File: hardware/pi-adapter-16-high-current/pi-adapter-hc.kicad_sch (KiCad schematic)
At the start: 33 parts, among them J1 Conn_02x02_Odd_Even, P1 CONN_01X04, P10 CONN_01X04, P11 CONN_01X04, P12 CONN_01X04, P13 CONN_01X04, P14 CONN_01X04, P15 CONN_01X04, P16 CONN_01X04, P17 5V, P2 CONN_01X04, P20 CONN_02X20, P21 I2C, P22 System SPI, P23 UART, P3 CONN_01X04, P30 +5V, P31 GND, P4 CONN_01X04, P5 CONN_01X04, P6 CONN_01X04, P7 CONN_01X04, P8 CONN_01X04, P9 CONN_01X04, U1 74AHCT245, U2 74AHCT245, U3 74AHCT245, U4 74AHCT245

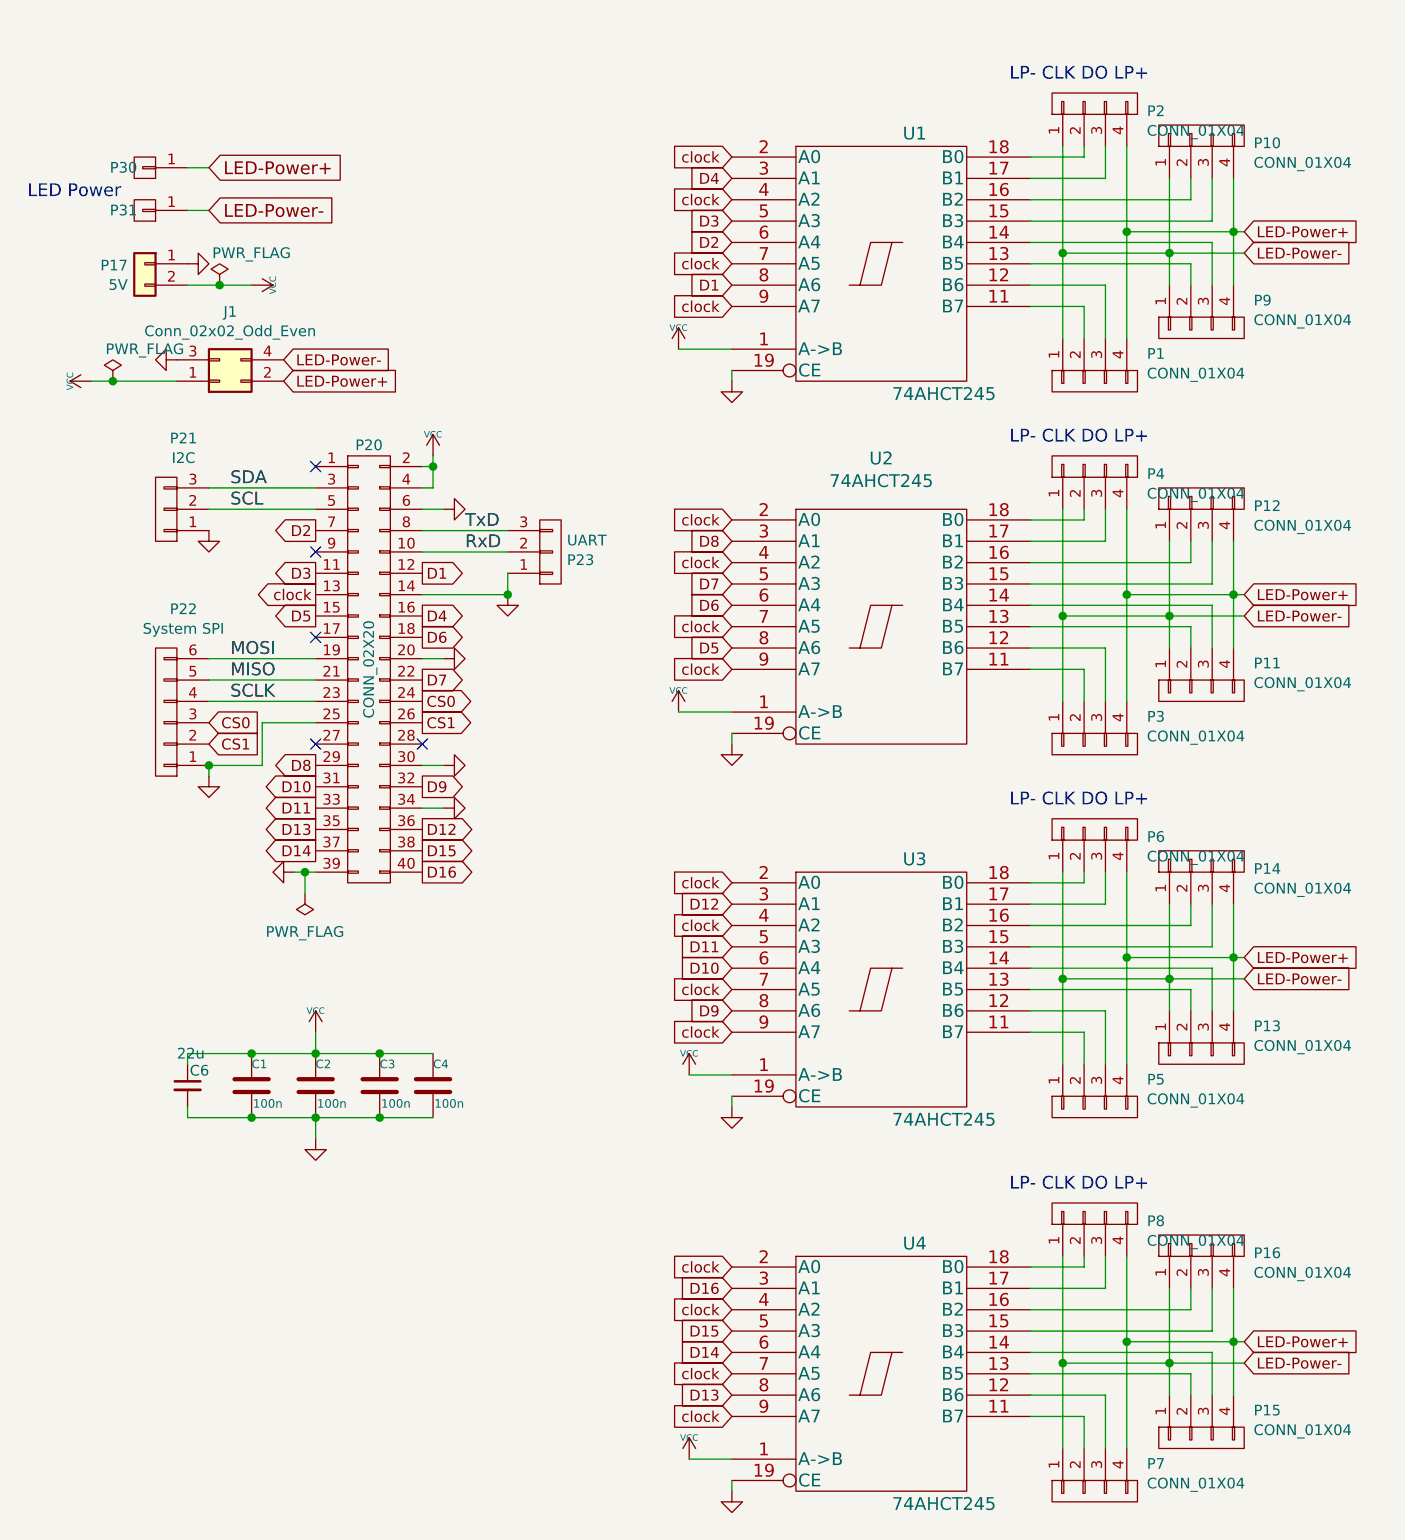
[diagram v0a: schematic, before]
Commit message: Update symbols and packages.
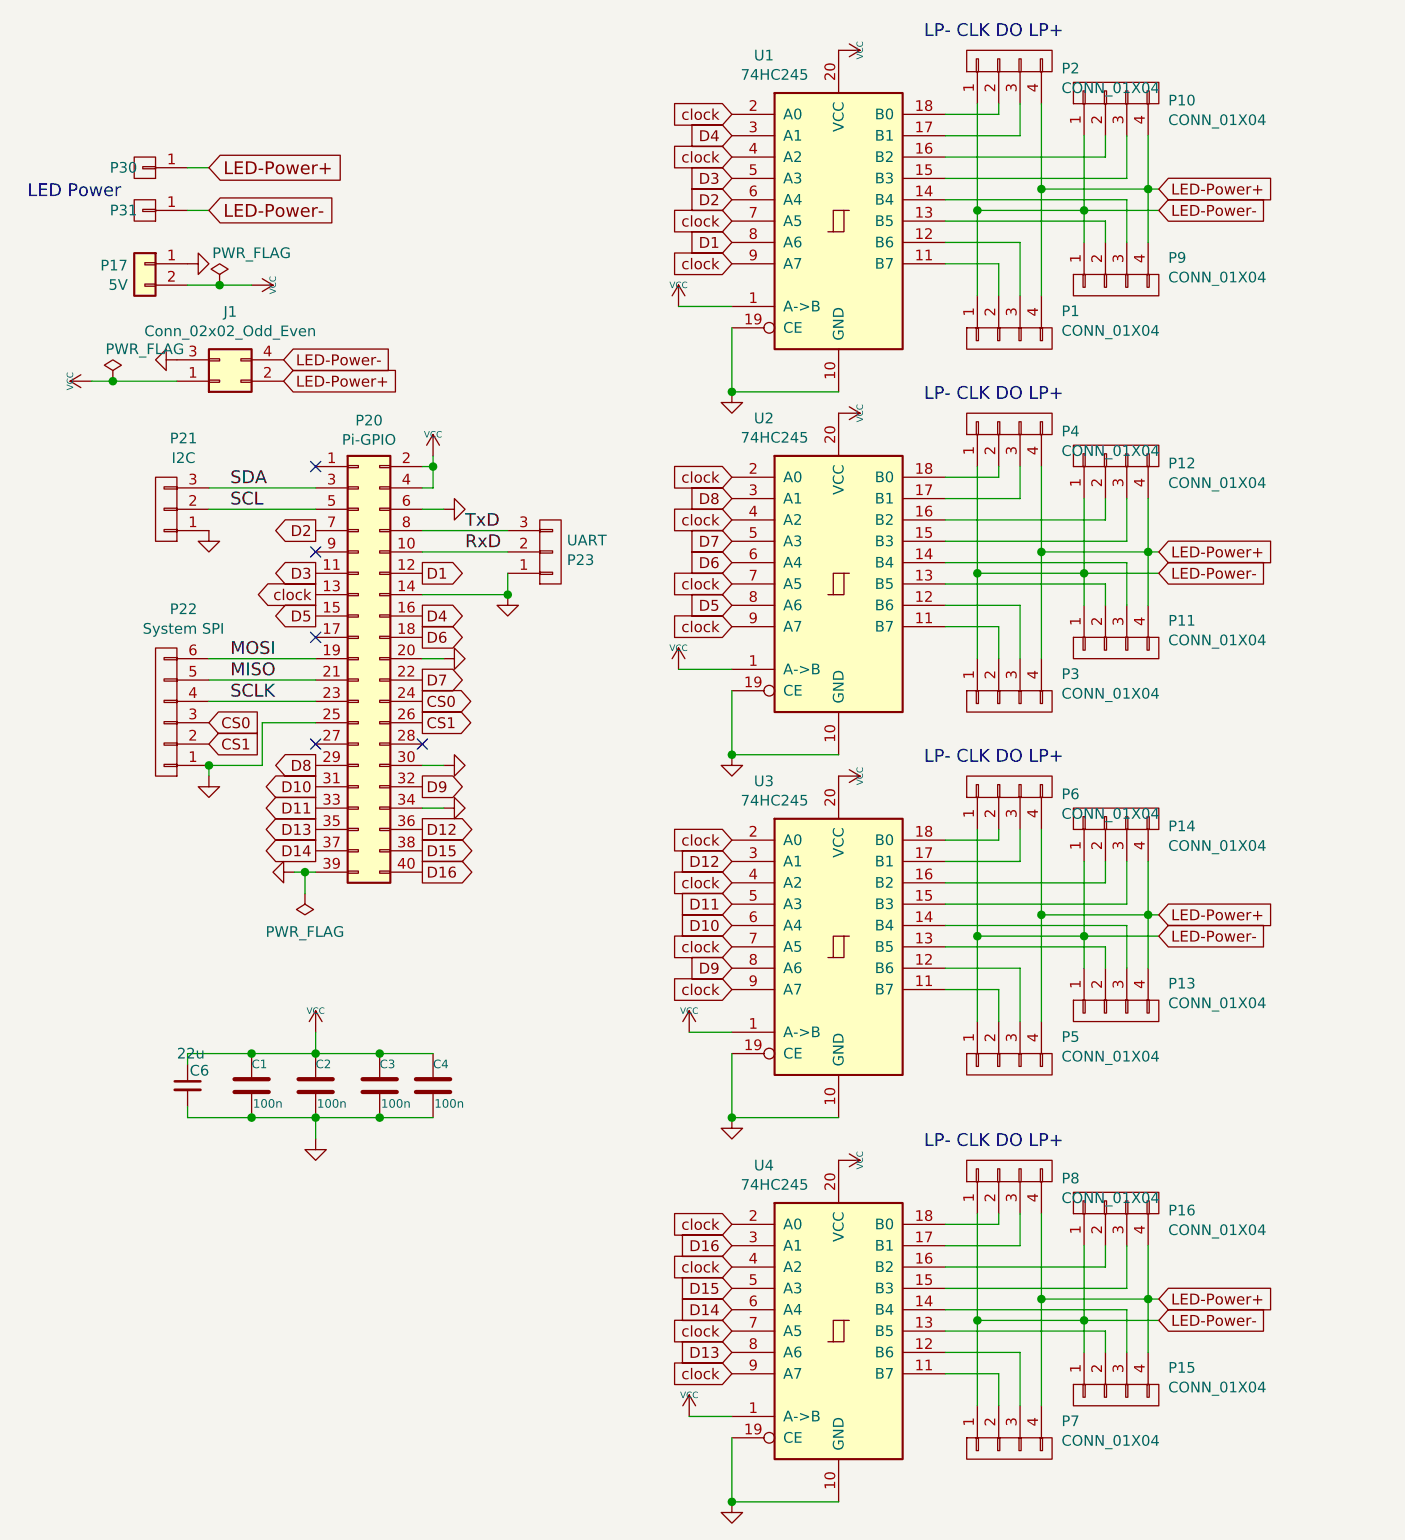
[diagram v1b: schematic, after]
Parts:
- removed P20: CONN_02X20, Pin_Headers:Pin_Header_Straight_2x20, symbol pi-adapter-rescue:CONN_02X20-RESCUE-pi-adapter
- removed U1, U2, U3, U4: 74AHCT245, Housings_SSOP:TSSOP-20_4.4x6.5mm_Pitch0.65mm, symbol pi-adapter-rescue:74HC245-RESCUE-pi-adapter
- added P20: Pi-GPIO, Connector_PinHeader_2.54mm:PinHeader_2x20_P2.54mm_Vertical, symbol Connector_Generic:Conn_02x20_Odd_Even
- added U1, U2, U3, U4: 74HC245, Package_SO:TSSOP-20_4.4x6.5mm_P0.65mm, symbol 74xx:74HC245
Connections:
- net CS0: now also P20.24 (Pin_24)
- net CS1: now also P20.26 (Pin_26)
- net D1: now also P20.12 (Pin_12), U1.8 (A6)
- net D10: now also P20.31 (Pin_31), U3.6 (A4)
- net D11: now also P20.33 (Pin_33), U3.5 (A3)
- net D12: now also P20.36 (Pin_36), U3.3 (A1)
- net D13: now also P20.35 (Pin_35), U4.8 (A6)
- net D14: now also P20.37 (Pin_37), U4.6 (A4)
- net D15: now also P20.38 (Pin_38), U4.5 (A3)
- net D16: now also P20.40 (Pin_40), U4.3 (A1)
- net D2: now also P20.7 (Pin_7), U1.6 (A4)
- net D3: now also P20.11 (Pin_11), U1.5 (A3)
- net D4: now also P20.16 (Pin_16), U1.3 (A1)
- net D5: now also P20.15 (Pin_15), U2.8 (A6)
- net D6: now also P20.18 (Pin_18), U2.6 (A4)
- net D7: now also P20.22 (Pin_22), U2.5 (A3)
- net D8: now also P20.29 (Pin_29), U2.3 (A1)
- net D9: now also P20.32 (Pin_32), U3.8 (A6)
- net GND: now also P20.14 (Pin_14), P20.20 (Pin_20), P20.25 (Pin_25), P20.30 (Pin_30), P20.34 (Pin_34), P20.39 (Pin_39), P20.6 (Pin_6), U1.10 (GND), U1.19 (CE), U2.10 (GND), U2.19 (CE), U3.10 (GND), U3.19 (CE), U4.10 (GND), U4.19 (CE)
- net MISO: now also P20.21 (Pin_21)
- net MOSI: now also P20.19 (Pin_19)
- net RxD: now also P20.10 (Pin_10)
- net SCL: now also P20.5 (Pin_5)
- net SCLK: now also P20.23 (Pin_23)
- net SDA: now also P20.3 (Pin_3)
- net TxD: now also P20.8 (Pin_8)
- net VCC: now also P20.2 (Pin_2), P20.4 (Pin_4), U1.1 (A->B), U1.20 (VCC), U2.1 (A->B), U2.20 (VCC), U3.1 (A->B), U3.20 (VCC), U4.1 (A->B), U4.20 (VCC)
- net clock: now also P20.13 (Pin_13), U1.2 (A0), U1.4 (A2), U1.7 (A5), U1.9 (A7), U2.2 (A0), U2.4 (A2), U2.7 (A5), U2.9 (A7), U3.2 (A0), U3.4 (A2), U3.7 (A5), U3.9 (A7), U4.2 (A0), U4.4 (A2), U4.7 (A5), U4.9 (A7)
- net at P1.2 (P2): now also U1.11 (B7)
- net at P1.3 (P3): now also U1.12 (B6)
- net at P9.2 (P2): now also U1.13 (B5)
- net at P9.3 (P3): now also U1.14 (B4)
- net at P10.3 (P3): now also U1.15 (B3)
- net at P10.2 (P2): now also U1.16 (B2)
- net at P2.3 (P3): now also U1.17 (B1)
- net at P2.2 (P2): now also U1.18 (B0)
- net at P3.2 (P2): now also U2.11 (B7)
- net at P3.3 (P3): now also U2.12 (B6)
- net at P11.2 (P2): now also U2.13 (B5)
- net at P11.3 (P3): now also U2.14 (B4)
- net at P12.3 (P3): now also U2.15 (B3)
- net at P12.2 (P2): now also U2.16 (B2)
- net at P4.3 (P3): now also U2.17 (B1)
- net at P4.2 (P2): now also U2.18 (B0)
- net at P5.2 (P2): now also U3.11 (B7)
- net at P5.3 (P3): now also U3.12 (B6)
- net at P13.2 (P2): now also U3.13 (B5)
- net at P13.3 (P3): now also U3.14 (B4)
- net at P14.3 (P3): now also U3.15 (B3)
- net at P14.2 (P2): now also U3.16 (B2)
- net at P6.3 (P3): now also U3.17 (B1)
- net at P6.2 (P2): now also U3.18 (B0)
- net at P7.2 (P2): now also U4.11 (B7)
- net at P7.3 (P3): now also U4.12 (B6)
- net at P15.2 (P2): now also U4.13 (B5)
- net at P15.3 (P3): now also U4.14 (B4)
- net at P16.3 (P3): now also U4.15 (B3)
- net at P16.2 (P2): now also U4.16 (B2)
- net at P8.3 (P3): now also U4.17 (B1)
- net at P8.2 (P2): now also U4.18 (B0)
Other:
- moved on the sheet: P1, P10, P11, P12, P13, P14, P15, P16, P2, P3, P4, P5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

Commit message: Separate LED power input for upper and lower bank.
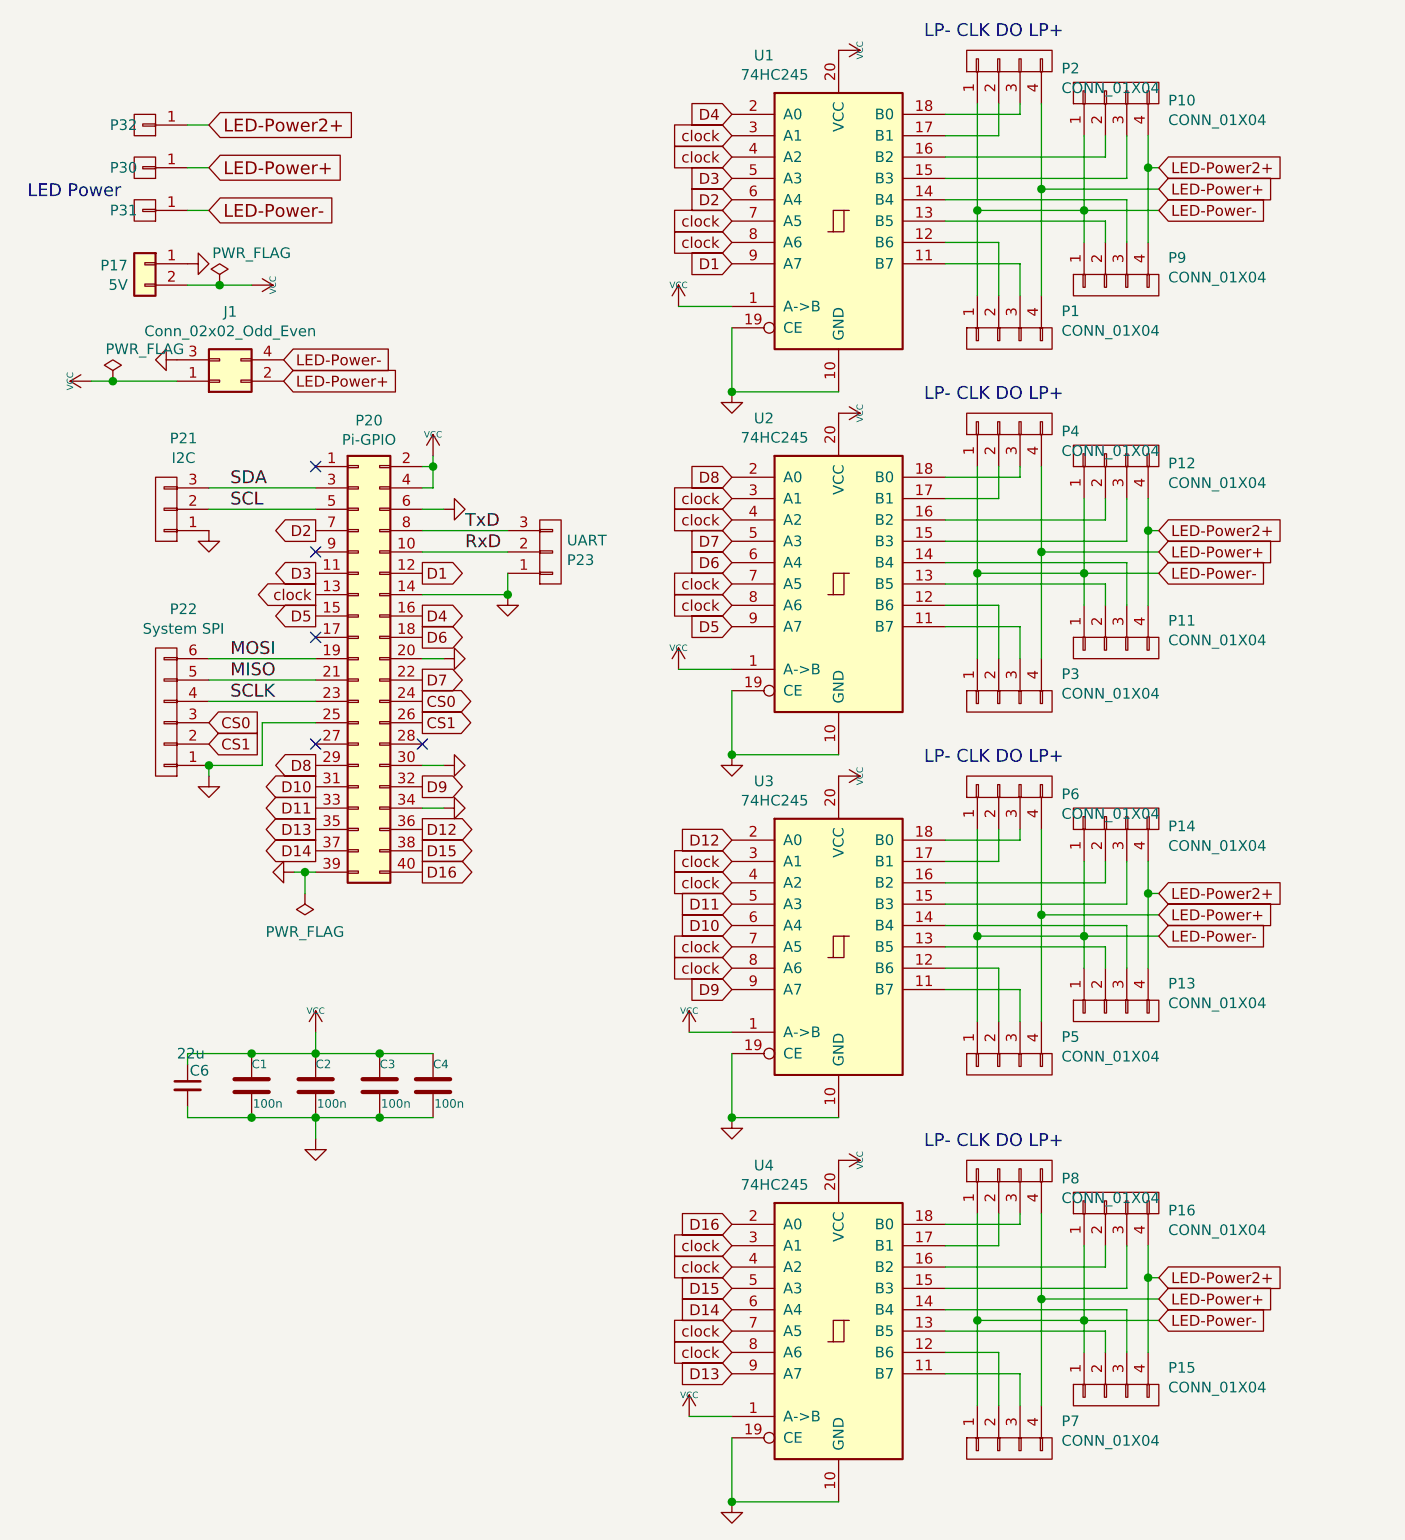
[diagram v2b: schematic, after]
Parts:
- added P32: +5V, Connector_PinHeader_1.00mm:PinHeader_1x01_P1.00mm_Vertical, symbol pi-adapter-rescue:CONN_01X01-RESCUE-pi-adapter
- P30, P31: footprint Pin_Headers:Pin_Header_Straight_1x01 -> Connector_PinHeader_1.00mm:PinHeader_1x01_P1.00mm_Vertical
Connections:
- net D1: now also U1.9 (A7); no longer U1.8 (A6)
- net D12: now also U3.2 (A0); no longer U3.3 (A1)
- net D13: now also U4.9 (A7); no longer U4.8 (A6)
- net D16: now also U4.2 (A0); no longer U4.3 (A1)
- net D4: now also U1.2 (A0); no longer U1.3 (A1)
- net D5: now also U2.9 (A7); no longer U2.8 (A6)
- net D8: now also U2.2 (A0); no longer U2.3 (A1)
- net D9: now also U3.9 (A7); no longer U3.8 (A6)
- net LED-Power+: no longer P10.4 (P4), P11.4 (P4), P12.4 (P4), P13.4 (P4), P14.4 (P4), P15.4 (P4), P16.4 (P4), P9.4 (P4)
- net clock: now also U1.3 (A1), U1.8 (A6), U2.3 (A1), U2.8 (A6), U3.3 (A1), U3.8 (A6), U4.3 (A1), U4.8 (A6); no longer U1.2 (A0), U1.9 (A7), U2.2 (A0), U2.9 (A7), U3.2 (A0), U3.9 (A7), U4.2 (A0), U4.9 (A7)
- net at P2.2 (P2): now also U1.17 (B1); no longer U1.18 (B0)
- net at P2.3 (P3): now also U1.18 (B0); no longer U1.17 (B1)
- net at P1.2 (P2): now also U1.12 (B6); no longer U1.11 (B7)
- net at P1.3 (P3): now also U1.11 (B7); no longer U1.12 (B6)
- net at P4.2 (P2): now also U2.17 (B1); no longer U2.18 (B0)
- net at P4.3 (P3): now also U2.18 (B0); no longer U2.17 (B1)
- net at P3.2 (P2): now also U2.12 (B6); no longer U2.11 (B7)
- net at P3.3 (P3): now also U2.11 (B7); no longer U2.12 (B6)
- net at P6.2 (P2): now also U3.17 (B1); no longer U3.18 (B0)
- net at P6.3 (P3): now also U3.18 (B0); no longer U3.17 (B1)
- net at P5.2 (P2): now also U3.12 (B6); no longer U3.11 (B7)
- net at P5.3 (P3): now also U3.11 (B7); no longer U3.12 (B6)
- net at P8.2 (P2): now also U4.17 (B1); no longer U4.18 (B0)
- net at P8.3 (P3): now also U4.18 (B0); no longer U4.17 (B1)
- net at P7.2 (P2): now also U4.12 (B6); no longer U4.11 (B7)
- net at P7.3 (P3): now also U4.11 (B7); no longer U4.12 (B6)
- new net LED-Power2+: P10.4 (P4), P11.4 (P4), P12.4 (P4), P13.4 (P4), P14.4 (P4), P15.4 (P4), P16.4 (P4), P32.1 (P1), P9.4 (P4)
